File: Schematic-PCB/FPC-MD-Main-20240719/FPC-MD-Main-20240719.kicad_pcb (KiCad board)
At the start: 2 copper layers, 100 x 16 mm, 2 parts, among them J1 Conn_01x15_Pin, J2 Conn_01x15_Pin

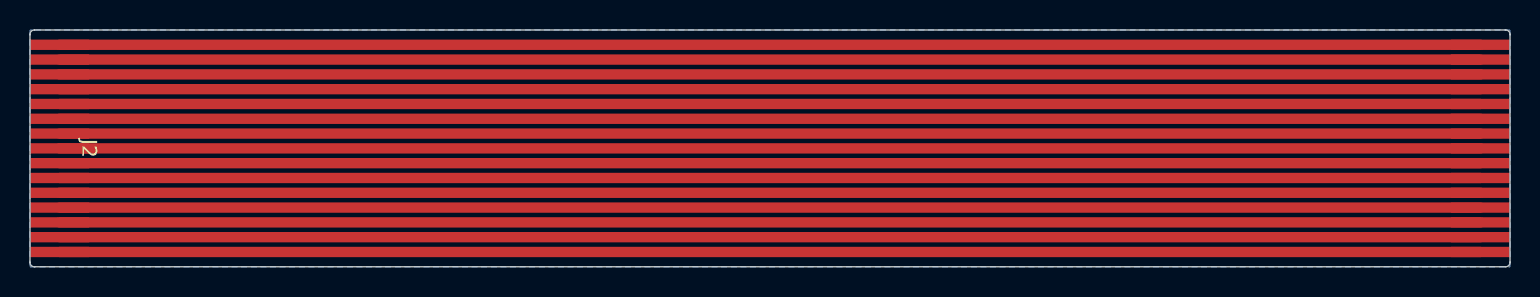
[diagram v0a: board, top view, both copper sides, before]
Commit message: update: FPCケーブル（旧）を裏表導通するように変更した
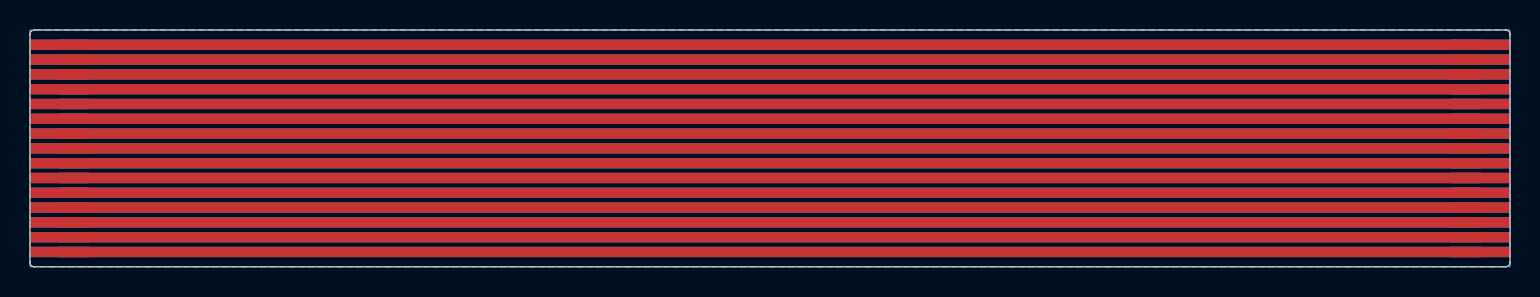
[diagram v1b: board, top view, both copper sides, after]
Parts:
- J1, J2: footprint @2024TOINIOT2-FPC-FFC:FPC-FFC -> @2024TOINIOT2-FPC-FCC:FPC-FFC
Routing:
- net Net-(J1-Pin_9): track 96.0 -> 192.0 mm
- net Net-(J1-Pin_8): track 96.0 -> 192.0 mm
- net Net-(J1-Pin_7): track 96.0 -> 192.0 mm
- net Net-(J1-Pin_6): track 96.0 -> 192.0 mm
- net Net-(J1-Pin_5): track 96.0 -> 192.0 mm
- net Net-(J1-Pin_4): track 96.0 -> 192.0 mm
- net Net-(J1-Pin_3): track 96.0 -> 192.0 mm
- net Net-(J1-Pin_2): track 96.0 -> 192.0 mm
- net Net-(J1-Pin_15): track 96.0 -> 192.0 mm
- net Net-(J1-Pin_14): track 96.0 -> 192.0 mm
- net Net-(J1-Pin_13): track 96.0 -> 192.0 mm
- net Net-(J1-Pin_12): track 96.0 -> 192.0 mm
- net Net-(J1-Pin_11): track 96.0 -> 192.0 mm
- net Net-(J1-Pin_10): track 96.0 -> 192.0 mm
- net Net-(J1-Pin_1): track 96.0 -> 192.0 mm
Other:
- board text added: "FPC | MD-Main | 002"
- board text removed: "FPC | MD-Main"

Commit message: update: FPCケーブルのPCBデザインを修正した
裏面のベタを削除して各個独立した配線になるようにした
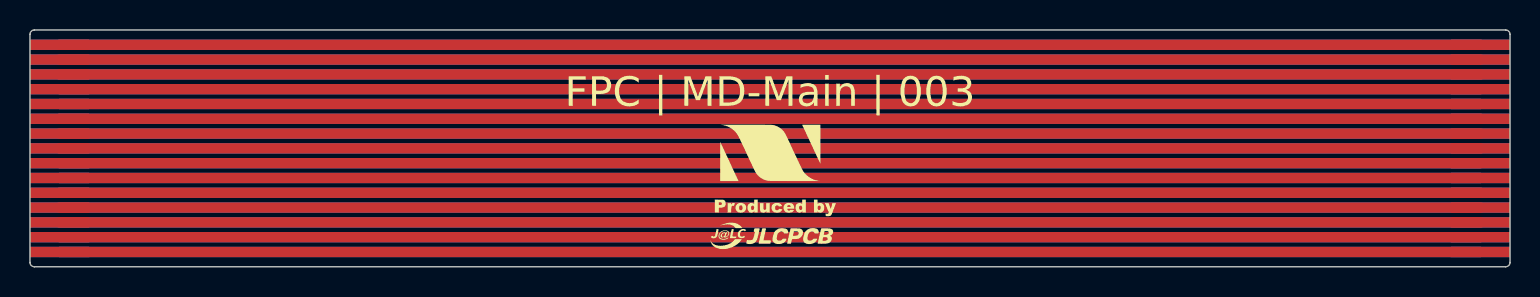
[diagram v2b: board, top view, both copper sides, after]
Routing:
- removed copper zone on B.Cu, net (none)
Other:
- board text added: "FPC | MD-Main | 003"
- board text removed: "FPC | MD-Main | 002"

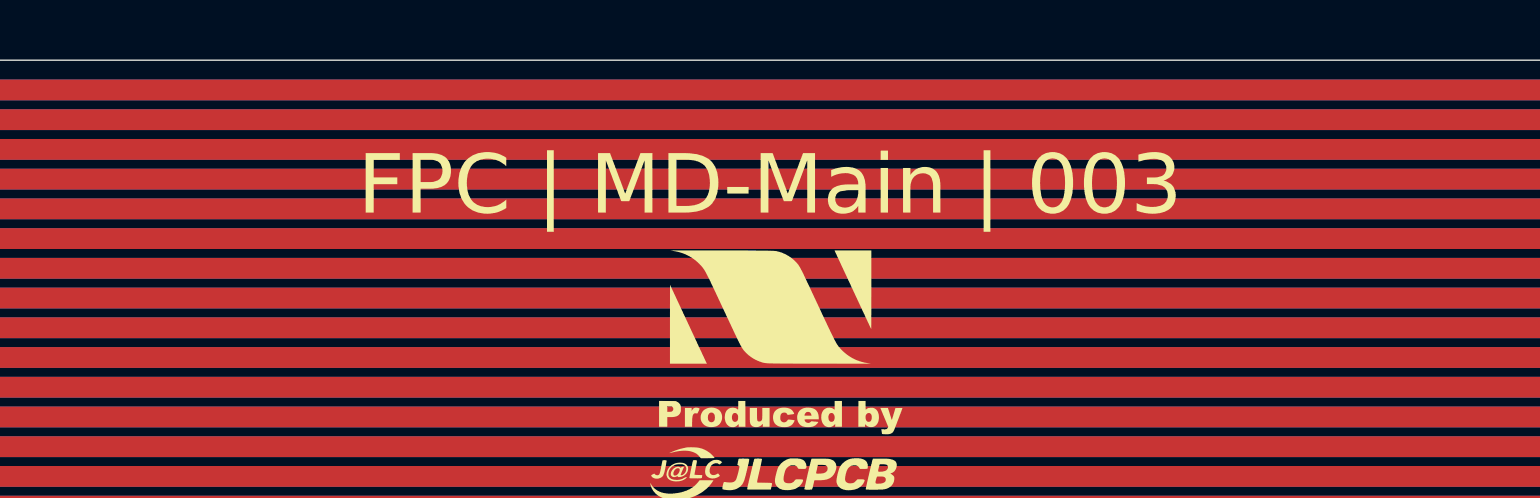
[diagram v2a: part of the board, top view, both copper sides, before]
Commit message: update: FPC ver.004 に更新した
プロジェクトファイル自体は一番初めのモノを使用してるよ
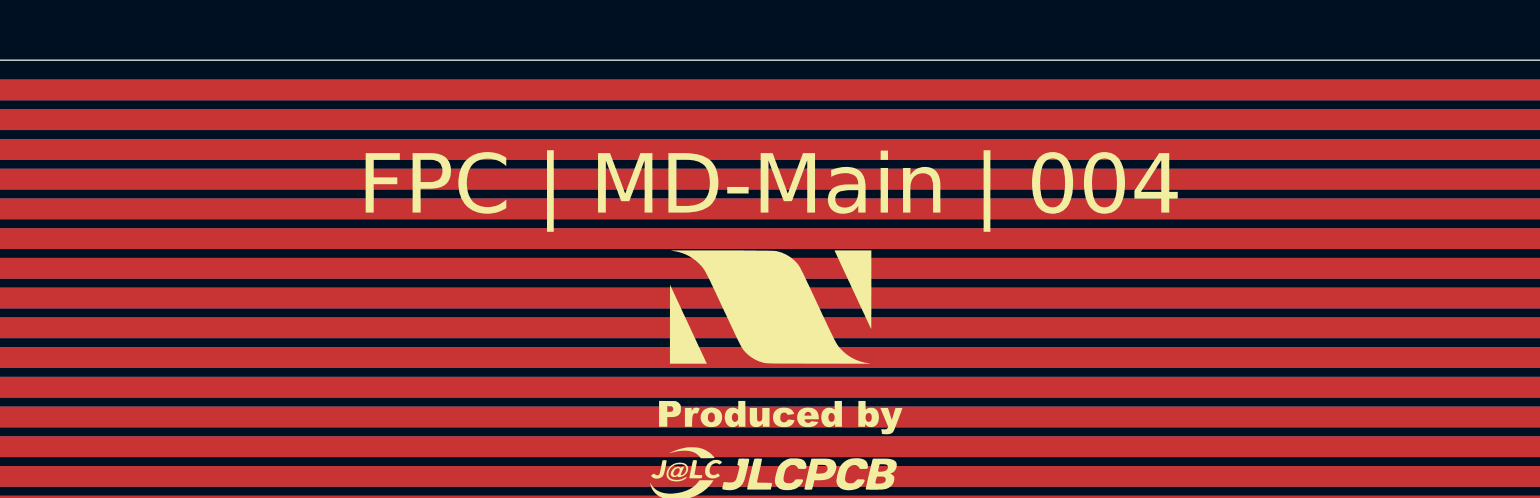
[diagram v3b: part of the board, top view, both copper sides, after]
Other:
- board text added: "FPC | MD-Main | 004"
- board text removed: "FPC | MD-Main | 003"
